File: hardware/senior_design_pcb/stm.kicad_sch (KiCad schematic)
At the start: 30 parts, among them J1 SBH11-PBPC-D05-ST-BK, SW1 SW_Push, U1 LD1117S33TR_SOT223, U2 STM32F091RCTx, X1 32.768kHz(12.5pF), X3 8MHz(20pF)

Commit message: pushing for the night
minor updates including adding more words and realigning things
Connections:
- net +3V0: now also U2.48 (VDDIO2), U2.64 (VDD); no longer U2.13 (VDDA)
- net 3VA: now also U2.13 (VDDA); no longer U2.64 (VDD)
- net BOOT0: now also U2.60 (PF11); no longer U2.25 (PC5)
- net GND: now also U2.12 (VSSA), U2.18 (VSS), U2.31 (VSS), U2.47 (VSS), U2.63 (VSS)
- net PC0: now also U2.8 (PC0); no longer U2.40 (PC9)
- net PC1: now also U2.9 (PC1); no longer U2.51 (PC10)
- net PC10: now also U2.51 (PC10)
- net PC11: now also U2.52 (PC11)
- net PC12: now also U2.53 (PC12)
- net PC13: now also U2.2 (PC13)
- net PC14: now also U2.3 (PC14)
- net PC15: now also U2.4 (PC15)
- net PC2: now also U2.10 (PC2); no longer U2.52 (PC11)
- net PC3: now also U2.11 (PC3); no longer U2.53 (PC12)
- net PC4: now also U2.24 (PC4); no longer U2.2 (PC13)
- net PC5: now also U2.25 (PC5); no longer U2.3 (PC14)
- net PC6: now also U2.37 (PC6); no longer U2.4 (PC15)
- net PC7: now also U2.38 (PC7)
- net PC8: now also U2.39 (PC8)
- net PC9: now also U2.40 (PC9)
- net PD2: now also U2.54 (PD2); no longer U2.38 (PC7)
- net PF0: now also U2.5 (PF0); no longer U2.11 (PC3)
- net PF1: now also U2.6 (PF1); no longer U2.24 (PC4)
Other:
- note added: "3V3 conversion"
- note added: "JST Conn"
- note added: "do not use as outputs"
- note added: "does it need power input from a non jst? it will always be plugged into the laptop"
- note added: "usb-ttl"
- moved on the sheet: C1, C2, C3, C4, C5, C6, C7, C8, C9, D1, D2, FB1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

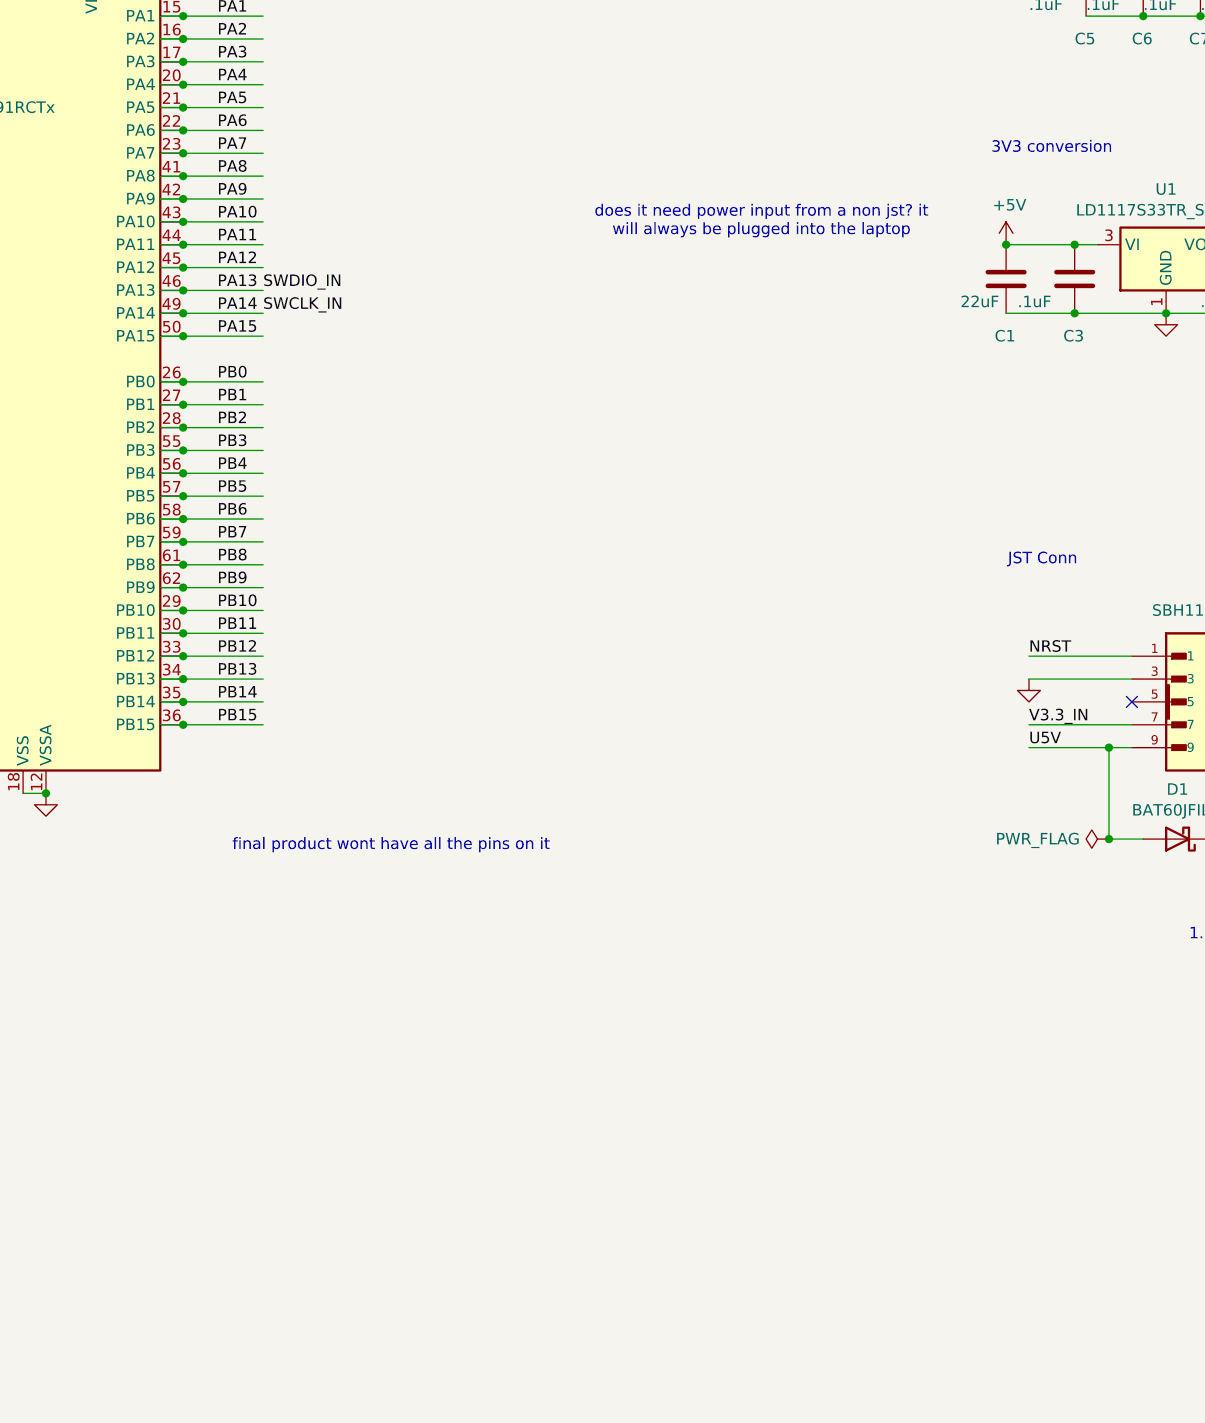
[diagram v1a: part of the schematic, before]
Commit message: ok actually pushing for the night
added usbc receptacle and labeled what would go where
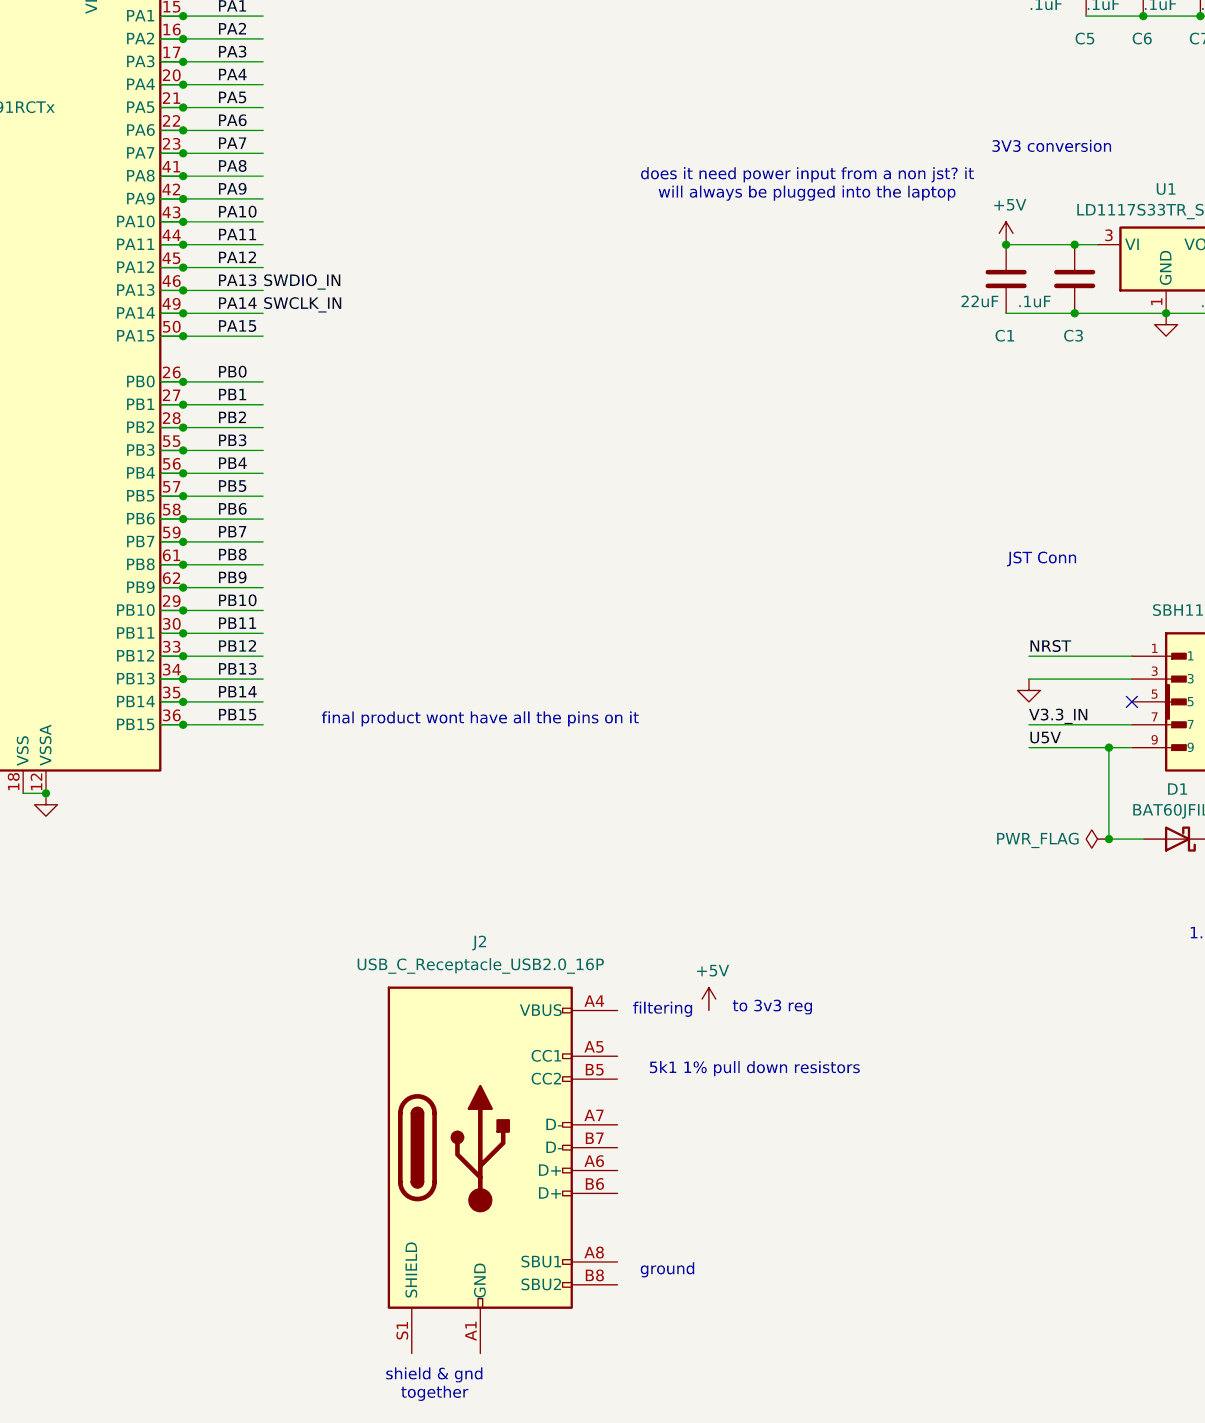
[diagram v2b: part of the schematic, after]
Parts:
- added J2: USB_C_Receptacle_USB2.0_16P, symbol Connector:USB_C_Receptacle_USB2.0_16P
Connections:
- new net: J2.A1 (GND), J2.A12 (GND), J2.B1 (GND), J2.B12 (GND)
- new net: J2.A4 (VBUS), J2.A9 (VBUS), J2.B4 (VBUS), J2.B9 (VBUS)
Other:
- note added: "5k1 1% pull down resistors"
- note added: "filtering"
- note added: "ground"
- note added: "shield & gnd together"
- note added: "to 3v3 reg"
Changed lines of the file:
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@@
 		(title "AutonAir STM")
 	)
+	(text "ground\n"
+		(exclude_from_sim no)
+		(at 130.048 177.546 0)
+		(effects
+			(font
+				(size 1.27 1.27)
+			)
+		)
+	)
 	(text "does it need power input from a non jst? it \nwill always be plugged into the laptop"
 		(exclude_from_sim no)
-		(at 140.462 60.96 0)
+		(at 145.542 56.896 0)
 		(effects
 			(font
@@
 		)
 	)
+	(text "5k1 1% pull down resistors"
+		(exclude_from_sim no)
+		(at 139.7 155.194 0)
+		(effects
+			(font
+				(size 1.27 1.27)
+			)
+		)
+	)
+	(text "shield & gnd\ntogether\n"
+		(exclude_from_sim no)
+		(at 104.14 190.246 0)
+		(effects
+			(font
+				(size 1.27 1.27)
+			)
+		)
+	)
 	(text "(nominal: 2.95 V)"
 		(exclude_from_sim no)
@@
 		)
 	)
+	(text "to 3v3 reg"
+		(exclude_from_sim no)
+		(at 141.732 148.336 0)
+		(effects
+			(font
+				(size 1.27 1.27)
+			)
+		)
+	)
 	(text "usb-ttl"
 		(exclude_from_sim no)
@@
 	(text "final product wont have all the pins on it\n"
 		(exclude_from_sim no)
-		(at 99.314 130.302 0)
+		(at 109.22 116.332 0)
+		(effects
+			(font
+				(size 1.27 1.27)
+			)
+		)
+	)
+	(text "filtering\n"
+		(exclude_from_sim no)
+		(at 129.54 148.59 0)
 		(effects
 			(font
@@
 	)
 	(symbol
+		(lib_id "power:+5V")
+		(at 134.62 148.59 0)
+		(unit 1)
+		(exclude_from_sim no)
+		(in_bom yes)
+		(on_board yes)
+		(dnp no)
+		(property "Reference" "#PWR01"
+			(at 134.62 152.4 0)
+			(effects
+				(font
+					(size 1.27 1.27)
+				)
+				(hide yes)
+			)
+		)
+		(property "Value" "+5V"
+			(at 135.001 144.1958 0)
+			(effects
+				(font
+					(size 1.27 1.27)
+				)
+			)
+		)
+		(property "Footprint" ""
+			(at 134.62 148.59 0)
+			(effects
+				(font
+					(size 1.27 1.27)
+				)
+				(hide yes)
+			)
+		)
+		(property "Datasheet" ""
+			(at 134.62 148.59 0)
+			(effects
+				(font
+					(size 1.27 1.27)
+				)
+				(hide yes)
+			)
+		)
+		(property "Description" ""
+			(at 134.62 148.59 0)
+			(effects
+				(font
+					(size 1.27 1.27)
+				)
+			)
+		)
+		(pin "1"
+		)
+		(instances
+			(project "senior_design_pcb"
+				(path "/50c554f9-3ed9-4f91-b5d3-2dee1756645e/595154cc-9bb5-4179-9279-e65ff803e35f"
+					(reference "#PWR01")
+					(unit 1)
+				)
+			)
+		)
+	)
+	(symbol
 		(lib_id "power:GND")
 		(at 262.89 120.65 0)
@@
 					(unit 1)
 				)
+			)
+		)
+	)
+	(symbol
+		(lib_id "Connector:USB_C_Receptacle_USB2.0_16P")
+		(at 109.22 163.83 0)
+		(unit 1)
+		(exclude_from_sim no)
+		(in_bom yes)
+		(on_board yes)
+		(dnp no)
+		(fields_autoplaced yes)
+		(property "Reference" "J2"
+			(at 109.22 140.97 0)
+			(effects
+				(font
+					(size 1.27 1.27)
+				)
+			)
+		)
+		(property "Value" "USB_C_Receptacle_USB2.0_16P"
+			(at 109.22 143.51 0)
+			(effects
+				(font
+					(size 1.27 1.27)
+				)
+			)
+		)
+		(property "Footprint" ""
+			(at 113.03 163.83 0)
+			(effects
+				(font
+					(size 1.27 1.27)
+				)
+				(hide yes)
+			)
+		)
+		(property "Datasheet" "https://www.usb.org/sites/default/files/documents/usb_type-c.zip"
+			(at 113.03 163.83 0)
+			(effects
+				(font
+					(size 1.27 1.27)
+				)
+				(hide yes)
+			)
+		)
+		(property "Description" "USB 2.0-only 16P Type-C Receptacle connector"
+			(at 109.22 163.83 0)
+			(effects
+				(font
+					(size 1.27 1.27)
+				)
+				(hide yes)
+			)
+		)
+		(pin "B8"
+		)
+		(pin "B4"
+		)
+		(pin "B6"
+		)
+		(pin "A6"
+		)
+		(pin "B12"
+		)
+		(pin "S1"
+		)
+		(pin "A8"
+		)
+		(pin "A7"
+		)
+		(pin "A9"
+		)
+		(pin "A4"
+		)
+		(pin "B9"
+		)
+		(pin "A5"
+		)
+		(pin "B5"
+		)
+		(pin "B7"
+		)
+		(pin "B1"
+		)
+		(pin "A12"
+		)
+		(pin "A1"
+		)
+		(instances
+			(project ""
+				(path "/50c554f9-3ed9-4f91-b5d3-2dee1756645e/595154cc-9bb5-4179-9279-e65ff803e35f"
+					(reference "J2")
+					(unit 1)
+				)

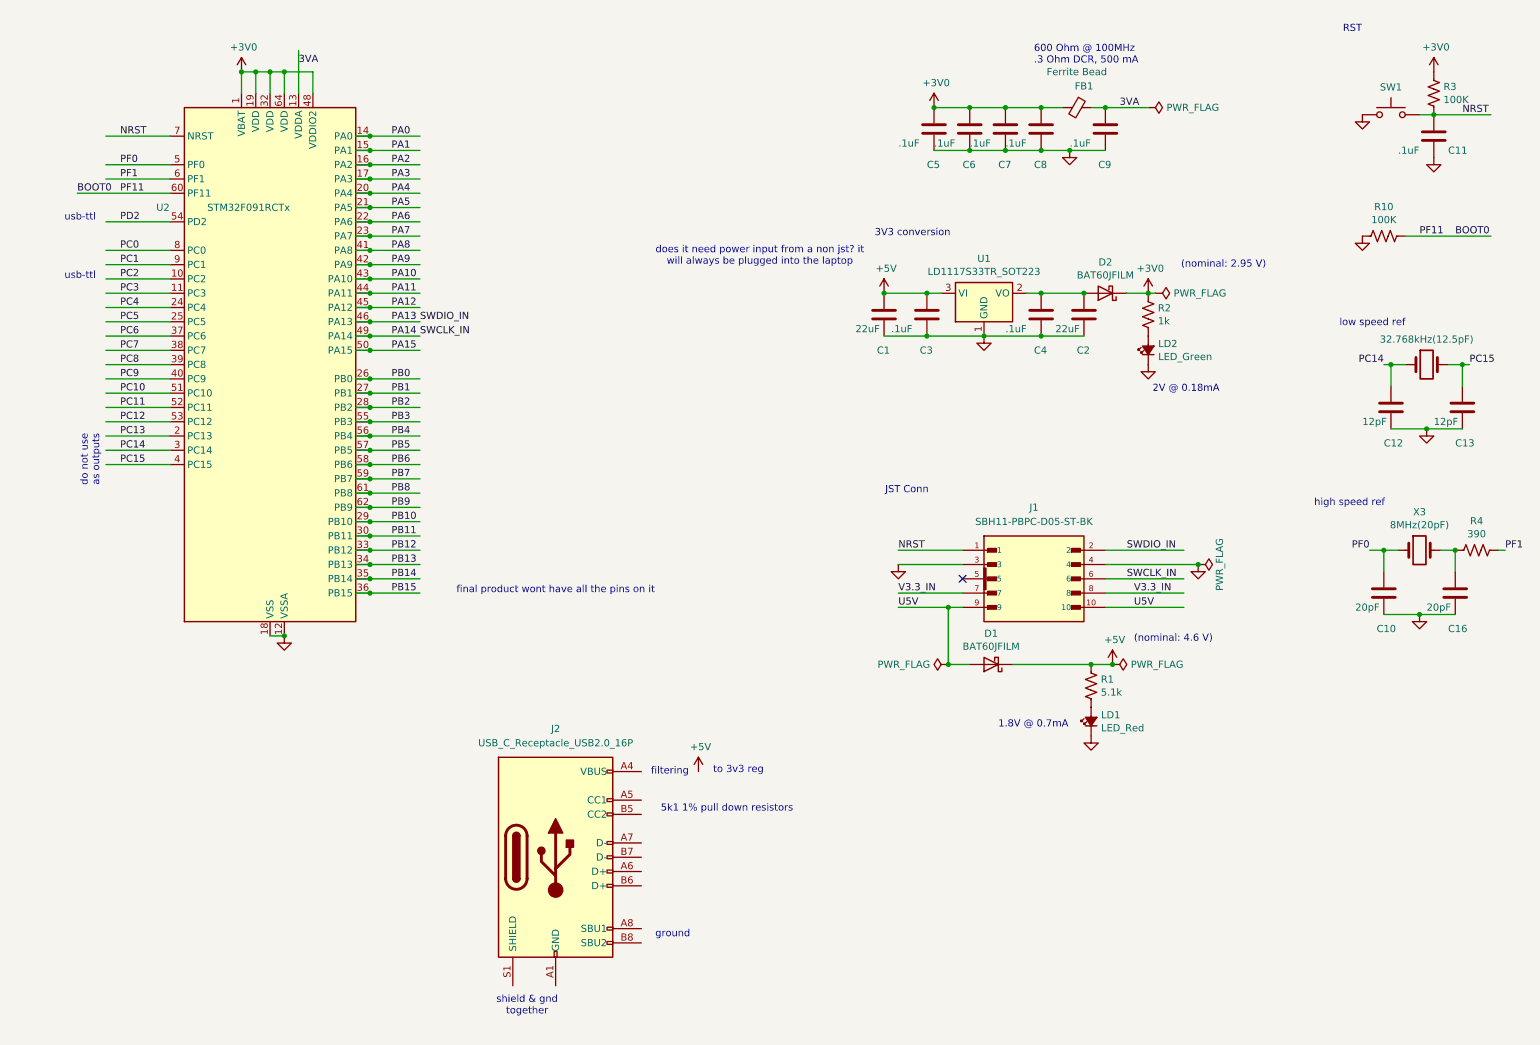
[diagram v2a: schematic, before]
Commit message: uart usb work
added filtering
added ft232 chip
added labels
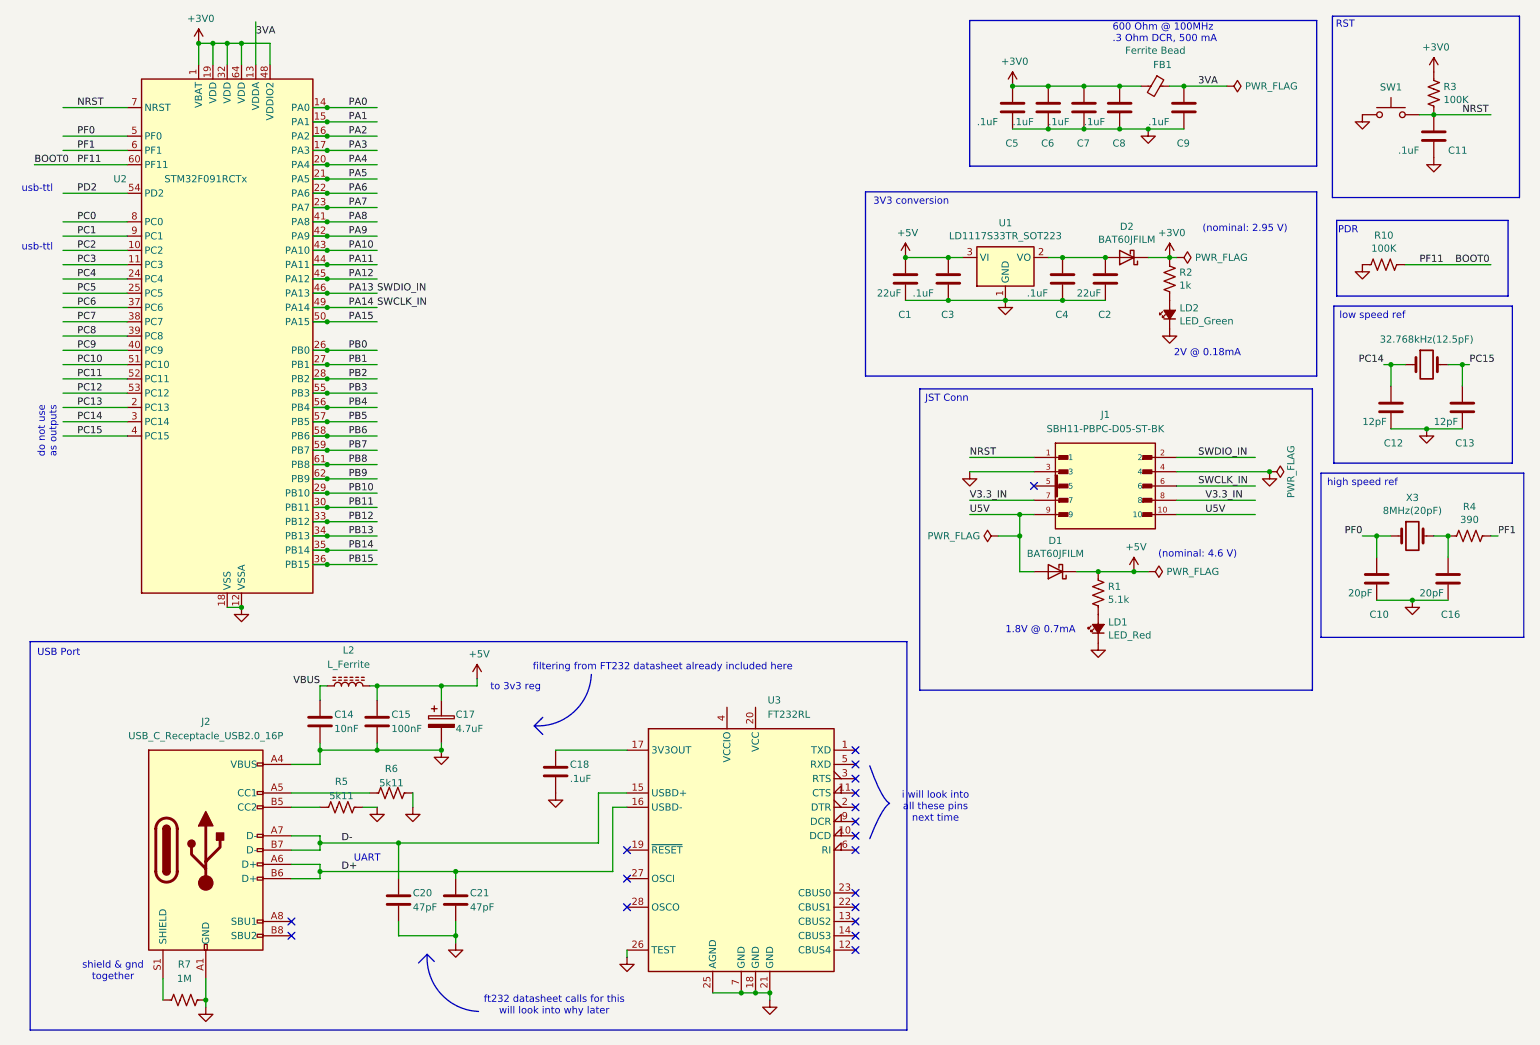
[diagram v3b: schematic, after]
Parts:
- added C14: 10nF, symbol Device:C
- added C15: 100nF, symbol Device:C
- added C17: 4.7uF, symbol Device:C_Polarized
- added C18: .1uF, symbol Device:C
- added C20, C21: 47pF, symbol Device:C
- added L2: L_Ferrite, symbol Device:L_Ferrite
- added R5, R6: 5k11, Resistor_SMD:R_0805_2012Metric, symbol Device:R_US
- added R7: 1M, Resistor_SMD:R_0805_2012Metric, symbol Device:R_US
- added U3: FT232RL, Package_SO:SSOP-28_5.3x10.2mm_P0.65mm, symbol Interface_USB:FT232RL
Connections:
- net +5V: now also C15.1, C17.1, L2.2
- net GND: now also J2.A1 (GND), J2.A12 (GND), J2.A4 (VBUS), J2.A9 (VBUS), J2.B1 (GND), J2.B12 (GND), J2.B4 (VBUS), J2.B9 (VBUS), C14.2, C15.2, C17.2, C18.2, C20.2, C21.2, R5.2, R6.2, R7.2, U3.18 (GND), U3.21 (GND), U3.25 (AGND), U3.26 (TEST), U3.7 (GND)
- net at J2.A5 (CC1): now also R6.1
- net D+: now reaches J2.A6 (D+)
- net D+: now also J2.B6 (D+), C21.1, U3.16 (USBD-)
- net D-: now reaches J2.A7 (D-)
- net D-: now also J2.B7 (D-), C20.1, U3.15 (USBD+)
- net at J2.B5 (CC2): now also R5.1
- net at J2.S1 (SHIELD): now also R7.1
- new net: C18.1, U3.17 (3V3OUT)
- new net VBUS: C14.1, L2.1
- no-connect marks 1 -> 19
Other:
- note added: "PDR"
- note added: "UART"
- note added: "USB Port"
- note added: "filtering from FT232 datasheet already included here"
- note added: "ft232 datasheet calls for this will look into why later"
- note added: "i will look into all these pins next time"
- note removed: "5k1 1% pull down resistors"
- note removed: "does it need power input from a non jst? it will always be plugged into the laptop"
- note removed: "filtering"
- note removed: "final product wont have all the pins on it"
- note removed: "ground"
- moved on the sheet: C1, C10, C16, C2, C3, C4, C5, C6, C7, C8, C9, D1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

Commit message: small progress on usbc
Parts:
- added R8, R9: 33, symbol Device:R_US
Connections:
- no-connect marks 19 -> 17
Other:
- note added: "aligns with FT232R usbc datasheet advice"
- note added: "i see people add these. it acts as a LF filter"
- note added: "the question is, do they go USB->C->R->MCU, or is it R->C in the middle? and, do i need them?"
- note removed: "ft232 datasheet calls for this will look into why later"
- moved on the sheet: C18
